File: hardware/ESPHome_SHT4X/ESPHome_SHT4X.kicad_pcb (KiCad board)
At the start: 2 copper layers, 50 x 30.6 mm, 43 parts, among them J2 UJ20-C-H-G-SMT-2A-P16-TR, SW1 SW_Push, SW2 SW_Push, SW3 SW_Push, U1 ESP32-C6-WROOM-1-N8, U2 BQ25628ERYKR, U3 SHT40-AD1F-R2, U4 XC6220B331MR-G

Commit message: making more progress
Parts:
- moved U3 2.73 mm to (134.6, 80.7)
- moved R3 0.72 mm to (156.7, 62.0), turned to 90 degrees
- moved R4 0.50 mm to (156.7, 64.2), turned to 90 degrees
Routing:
- net IO18: track 1.92 -> 45.1 mm, vias 0 -> 2
- net VBUS: track 8.42 -> 33.6 mm, vias 0 -> 2
- net SDA: track 15.6 -> 37.9 mm, vias 0 -> 2
- net SCL: track 15.7 -> 37.6 mm, vias 0 -> 2
- net Net-(U2-STAT): track 0.00 -> 13.9 mm, vias 0 -> 2
- net SYS: track 24.6 -> 37.1 mm, vias 0 -> 2
- net ESP_3V3: track 106.8 -> 118.3 mm, vias 4 -> 7
- net GND: track 15.9 -> 22.3 mm, vias 8 -> 43
- net BTST: track 0.00 -> 2.45 mm
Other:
- outline, holes or cut-outs redrawn

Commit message: making more progress
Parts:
- U2: footprint Library:WQFN-HR18__RYK_TEX -> ESPhome:WQFN-HR18__RYK_TEX
- moved C4 10.9 mm to (144.5, 68.8)
- moved C10 8.42 mm to (142.9, 68.7), turned to 180 degrees
- moved C5 7.48 mm to (145.9, 68.3), turned to 0 degrees
- moved L1 7.43 mm to (150.0, 71.2), turned to -90 degrees
- moved C9 7.17 mm to (142.1, 71.3), turned to 180 degrees
- moved R8 7.00 mm to (142.1, 72.4), turned to 0 degrees
- moved C6 6.64 mm to (145.9, 69.2), turned to 0 degrees
- moved R15 6.56 mm to (148.9, 70.1), turned to 90 degrees
- moved C8 6.39 mm to (148.2, 74.8), turned to -90 degrees
- moved C7 5.86 mm to (144.7, 75.3), turned to 180 degrees
- moved U2 0.83 mm to (145.4, 71.7), turned to 0 degrees
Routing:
- net ESP_3V3: track 118.3 -> 46.7 mm
- net IO18: track 45.1 -> 0.00 mm, vias 2 -> 0
- net *INT: track 47.1 -> 2.86 mm, vias 2 -> 0
- net SYS: track 37.1 -> 0.00 mm, vias 2 -> 8
- net VBUS: track 33.6 -> 6.54 mm, vias 2 -> 0
- net SCL: track 37.6 -> 17.5 mm
- net SDA: track 37.9 -> 19.7 mm
- net Net-(U2-STAT): track 13.9 -> 0.00 mm, vias 2 -> 1
- net *QON: track 13.4 -> 0.00 mm
- net Net-(U2-*PG): track 11.7 -> 0.00 mm
- net SW: track 8.67 -> 0.00 mm
- net GND: track 22.3 -> 16.8 mm, vias 43 -> 45
- net PMID: track 3.28 -> 0.00 mm
- net BTST: track 2.45 -> 0.00 mm
- net BAT: track 1.65 -> 0.00 mm
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- added copper zone on F.Cu, net BAT
- added copper zone on F.Cu, net Net-(U2-STAT)
- added copper zone on B.Cu, net SYS
- added copper zone on F.Cu, net SYS

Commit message: Continued work on PCB Layout
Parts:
- moved D2 3.35 mm to (144.2, 82.2)
- moved R6 3.35 mm to (144.1, 78.9)
- moved D1 3.35 mm to (147.5, 82.2)
- moved R5 3.35 mm to (147.4, 78.9)
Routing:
- net SYS: track 0.00 -> 19.0 mm
- net *QON: track 0.00 -> 10.2 mm, vias 0 -> 2
- net Net-(U2-*PG): track 0.00 -> 7.90 mm
- net Net-(U2-STAT): track 0.00 -> 6.59 mm, vias 1 -> 2

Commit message: Continued work on PCB Layout
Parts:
- moved C10 1.16 mm to (142.4, 69.8), turned to 0 degrees
- moved C7 0.81 mm to (145.0, 74.5)
- moved C4 0.52 mm to (144.0, 68.9), turned to 180 degrees
- moved C5 0.25 mm to (145.9, 68.1)
- moved C6 0.25 mm to (145.9, 68.9)
- moved R12 0.06 mm to (176.8, 76.0)
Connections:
- U1 pad 19: IO19 -> IO21
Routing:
- net *INT: track 2.86 -> 52.9 mm
- net IO18: track 0.00 -> 42.2 mm, vias 0 -> 2
- net SCL: track 17.5 -> 59.2 mm, vias 2 -> 4
- net SDA: track 19.7 -> 58.4 mm, vias 2 -> 3
- net ESP_3V3: track 46.7 -> 85.3 mm, vias 7 -> 8
- net VBUS: track 6.54 -> 28.3 mm
- net SYS: track 19.0 -> 34.8 mm
- net SW: track 0.00 -> 9.76 mm, vias 0 -> 3
- net Net-(U1-IO9): track 1.90 -> 6.77 mm, vias 0 -> 2
- net Net-(U2-*PG): track 7.90 -> 12.1 mm, vias 0 -> 2
- net PMID: track 0.00 -> 2.80 mm
- net GND: track 16.8 -> 15.0 mm, vias 45 -> 95
- net ILIM: track 0.00 -> 1.69 mm
- net Net-(U2-REGN): track 0.00 -> 1.55 mm
- net IO21: track 0.00 -> 0.58 mm
- added copper zone on F.Cu, net BTST
- added copper zone on F.Cu, net VBUS

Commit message: Continued work on PCB Layout
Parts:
- added REF**: MountingHole_2.7mm_M2.5_DIN965_Pad, MountingHole:MountingHole_2.7mm_M2.5_DIN965_Pad, F.Cu at (148.5, 62.1)
- added REF**: MountingHole_2.7mm_M2.5_DIN965_Pad, MountingHole:MountingHole_2.7mm_M2.5_DIN965_Pad, F.Cu at (181.2, 81.9)
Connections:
- U1 pad 30_1: (no net) -> GND
- U1 pad 30_10: (no net) -> GND
- U1 pad 30_11: (no net) -> GND
- U1 pad 30_12: (no net) -> GND
- U1 pad 30_2: (no net) -> GND
- U1 pad 30_3: (no net) -> GND
- U1 pad 30_4: (no net) -> GND
- U1 pad 30_5: (no net) -> GND
- U1 pad 30_6: (no net) -> GND
- U1 pad 30_7: (no net) -> GND
- U1 pad 30_8: (no net) -> GND
- U1 pad 30_9: (no net) -> GND
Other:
- board size 50 x 30.6 mm -> 54.3 x 30.6 mm

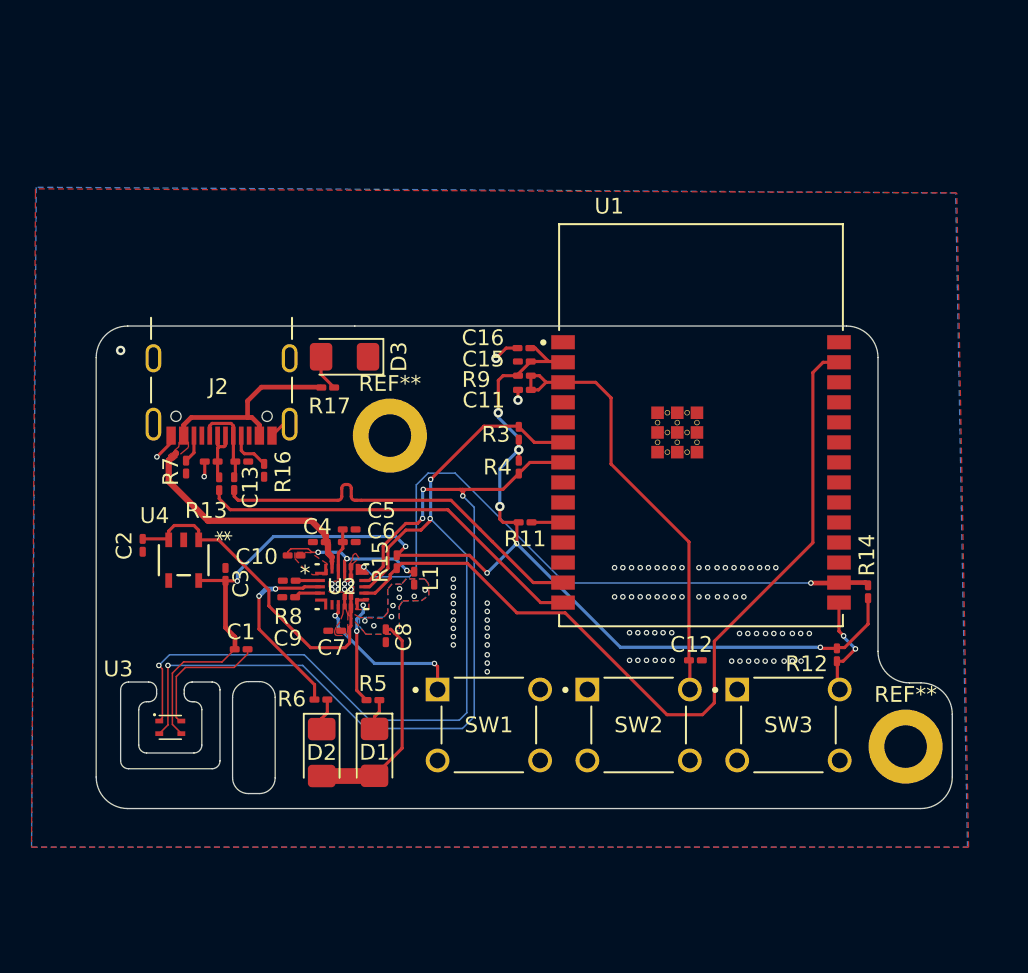
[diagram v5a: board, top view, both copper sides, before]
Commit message: Revamp of PCB Design to enable smaller overall footprint and less crossing of layers. Removed *QON button to reduce footprint size
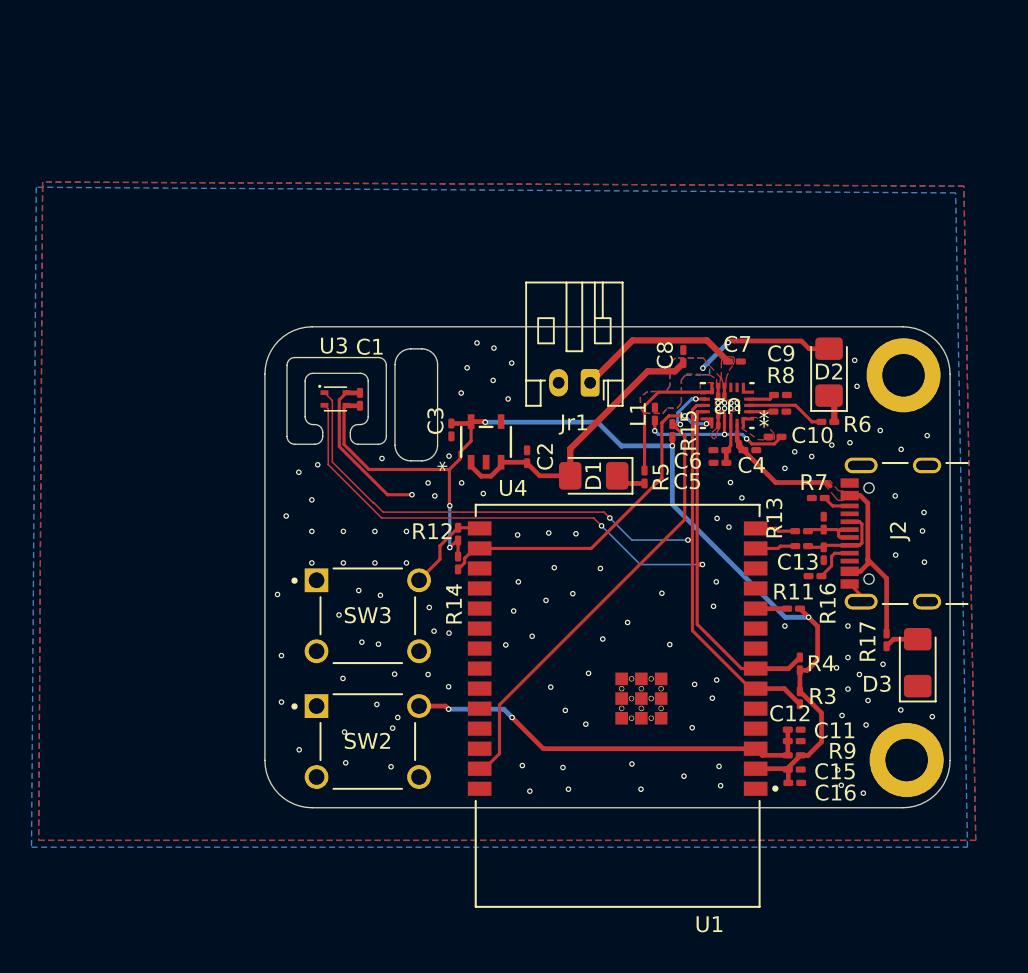
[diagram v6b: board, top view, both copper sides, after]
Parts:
- removed SW1: SW_Push, Library:SW_TS02-66-43-BK-100-SCR-D
- added Jr1: Conn_01x02_Pin, Connector_JST:JST_PH_S2B-PH-K_1x02_P2.00mm_Horizontal, F.Cu at (161.2, 58.8)
- moved J2 46.1 mm to (182.5, 68.4), turned to 90 degrees
- moved D3 41.2 mm to (181.9, 76.5), turned to 90 degrees
- moved D2 40.2 mm to (176.3, 58.1), turned to 90 degrees
- moved R7 40.1 mm to (175.6, 66.1), turned to 180 degrees
- moved C14 39.0 mm to (176.0, 67.7), turned to 90 degrees
- moved R17 38.9 mm to (180.0, 75.1), turned to 90 degrees
- moved C13 37.4 mm to (176.0, 69.6), turned to -90 degrees
- moved R13 37.1 mm to (174.6, 68.2), turned to 0 degrees
- moved R6 36.7 mm to (176.2, 61.3)
- moved R10 36.2 mm to (174.6, 69.2), turned to 0 degrees
- moved R16 35.6 mm to (175.4, 71.1), turned to 180 degrees
- moved R8 33.7 mm to (173.2, 59.6), turned to 180 degrees
- moved C9 32.9 mm to (173.2, 60.6), turned to 0 degrees
- moved REF** 32.8 mm to (181.1, 58.3)
- moved C16 32.5 mm to (174.2, 84.2), turned to 0 degrees
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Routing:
- net Net-(U1-IO12): track 25.1 -> 2.57 mm
- net Net-(U1-IO13): track 25.1 -> 2.59 mm
- net *INT: track 52.9 -> 31.2 mm, vias 0 -> 2
- net IO18: track 42.2 -> 23.3 mm
- net ESP_3V3: track 85.3 -> 67.7 mm, vias 8 -> 5
- net BAT: track 0.00 -> 10.4 mm
- net *QON: track 10.4 -> 0.00 mm, vias 2 -> 0
- net VBUS: track 28.3 -> 20.0 mm
- net Net-(U2-*PG): track 12.1 -> 5.03 mm, vias 2 -> 0
- net SYS: track 34.8 -> 27.7 mm, vias 8 -> 2
- net SCL: track 59.2 -> 52.5 mm, vias 4 -> 2
- net SDA: track 58.4 -> 53.3 mm, vias 3 -> 2
- net GND: track 15.0 -> 12.2 mm, vias 95 -> 125
- net Net-(U2-STAT): track 6.41 -> 8.73 mm, vias 2 -> 0
- net EN: track 28.3 -> 26.3 mm, vias 0 -> 2
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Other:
- board size 54.3 x 30.6 mm -> 43.4 x 30.5 mm

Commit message: Working
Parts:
- removed SW2, SW3: SW_Push, Library:SW_TS02-66-43-BK-100-SCR-D
- added S1: TS02-66-43-BK-100-SCR-D, Library:SW_TS02-66-43-BK-100-SCR-D, F.Cu at (147.0, 81.5)
- added S2: TS02-66-43-BK-100-SCR-D, Library:SW_TS02-66-43-BK-100-SCR-D, F.Cu at (147.0, 72.8)
- moved L1 3.15 mm to (167.4, 58.5), turned to 0 degrees
- moved C10 0.98 mm to (171.9, 62.3), turned to 0 degrees
- moved C5 0.83 mm to (169.4, 63.0), turned to -90 degrees
- moved C6 0.68 mm to (170.1, 63.0), turned to -90 degrees
- moved C8 0.08 mm to (167.0, 57.1)
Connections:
- J2 pad A7: D+ -> D-
- J2 pad B6: D- -> D+
- U1 pad 30_1: GND -> (no net)
- U1 pad 30_10: GND -> (no net)
- U1 pad 30_11: GND -> (no net)
- U1 pad 30_12: GND -> (no net)
- U1 pad 30_2: GND -> (no net)
- U1 pad 30_3: GND -> (no net)
- U1 pad 30_4: GND -> (no net)
- U1 pad 30_6: GND -> (no net)
- U1 pad 30_7: GND -> (no net)
- U1 pad 30_8: GND -> (no net)
- U1 pad 30_9: GND -> (no net)
- U1 pad r: GND -> (no net)
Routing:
- net EN: track 26.3 -> 32.8 mm
- net Net-(U1-IO9): track 6.42 -> 12.7 mm
- net SYS: track 27.7 -> 31.9 mm
- net SW: track 10.1 -> 8.02 mm
- net BTST: track 0.00 -> 2.05 mm
- net D+: track 3.82 -> 5.22 mm
- net D-: track 5.59 -> 4.38 mm
- net Net-(U2-STAT): track 8.73 -> 7.67 mm
- net GND: track 12.2 -> 13.0 mm, vias 125 -> 123
- net PMID: track 2.80 -> 2.16 mm
- removed copper zone on F.Cu, net BTST
- removed copper zone on B.Cu, net SYS
- removed copper zone on F.Cu, net SYS

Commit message: Working
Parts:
- moved D3 44.3 mm to (160.7, 37.7), turned to 180 degrees
- moved R17 41.0 mm to (159.2, 39.7), turned to 180 degrees
- moved J2 28.0 mm to (157.2, 56.6), turned to 180 degrees
- moved D1 27.1 mm to (151.7, 39.4)
- moved R5 27.1 mm to (154.9, 39.5)
- moved R15 24.9 mm to (152.5, 82.5), turned to 90 degrees
- moved C3 23.5 mm to (174.9, 68.6), turned to 0 degrees
- moved Jr1 23.2 mm to (180.5, 71.6), turned to 90 degrees
- moved U4 21.4 mm to (175.6, 66.4), turned to 180 degrees
- moved R7 20.9 mm to (154.9, 63.5), turned to -90 degrees
- moved C13 20.8 mm to (156.2, 63.1), turned to 180 degrees
- moved C2 19.4 mm to (176.6, 63.8), turned to 180 degrees
- moved R10 18.6 mm to (156.6, 64.5), turned to 90 degrees
- moved C14 18.5 mm to (158.0, 63.1), turned to 0 degrees
- moved R13 17.3 mm to (157.7, 64.5), turned to 90 degrees
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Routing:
- net Net-(U2-*PG): track 5.03 -> 30.5 mm
- net *INT: track 31.2 -> 8.83 mm
- net SYS: track 31.9 -> 11.6 mm, vias 2 -> 0
- net IO18: track 23.3 -> 6.28 mm, vias 2 -> 1
- net Net-(U1-IO12): track 2.57 -> 16.9 mm
- net Net-(U1-IO13): track 2.59 -> 16.8 mm
- net BAT: track 10.4 -> 0.00 mm
- net SW: track 8.02 -> 0.00 mm, vias 3 -> 10
- net Net-(U2-STAT): track 7.67 -> 0.00 mm, vias 0 -> 1
- net GND: track 13.0 -> 7.78 mm, vias 123 -> 21
- net SDA: track 53.3 -> 58.5 mm
- net ESP_3V3: track 67.8 -> 62.8 mm, vias 5 -> 0
- net SCL: track 52.5 -> 55.9 mm
- net D+: track 5.22 -> 2.74 mm
- net Net-(D3-A): track 2.16 -> 0.00 mm
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- added copper zone on F.Cu, net PMID
- added copper zone on B.Cu, net SW
- added copper zone on F.Cu, net SW
- added copper zone on F.Cu, net SYS
- removed copper zone on F.Cu, net Net-(U2-STAT)
- removed copper zone on F.Cu, net VBUS
